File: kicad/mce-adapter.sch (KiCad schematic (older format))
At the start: 18 parts, among them U1 GAL16V8

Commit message: Add necroware kicad library
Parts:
- PWR1: footprint MyLibrary:USB_Mini-B-Jing_Extension_LSCS_C46398 -> Necroware:USB_Mini-B-Jing_Extension_LSCS_C46398
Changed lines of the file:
@@
 F 0 "PWR1" H 3657 1817 50  0000 C CNN
 F 1 "USB_B_Mini" H 3657 1726 50  0000 C CNN
-F 2 "MyLibrary:USB_Mini-B-Jing_Extension_LSCS_C46398" H 3750 1300 50  0001 C CNN
+F 2 "Necroware:USB_Mini-B-Jing_Extension_LSCS_C46398" H 3750 1300 50  0001 C CNN
 F 3 "~" H 3750 1300 50  0001 C CNN
 F 4 "C46398" H 3600 1350 50  0001 C CNN "LCSC"

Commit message: Vastly shrink PCB
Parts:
- R1, R2, R3: value 330 -> 470
- R4, R5, R6: value 220 -> 330
- renumbered JP1-3 to J123, JP4 to J4
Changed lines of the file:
@@
 P 5300 2750
 F 0 "R6" V 5250 2600 50  0000 C CNN
-F 1 "220" V 5300 2750 50  0000 C CNN
+F 1 "330" V 5300 2750 50  0000 C CNN
 F 2 "Resistor_THT:R_Axial_DIN0204_L3.6mm_D1.6mm_P7.62mm_Horizontal" V 5230 2750 50  0001 C CNN
 F 3 "~" H 5300 2750 50  0001 C CNN
@@
 P 4900 2650
 F 0 "R3" V 4850 2500 50  0000 C CNN
-F 1 "330" V 4900 2650 50  0000 C CNN
+F 1 "470" V 4900 2650 50  0000 C CNN
 F 2 "Resistor_THT:R_Axial_DIN0204_L3.6mm_D1.6mm_P7.62mm_Horizontal" V 4830 2650 50  0001 C CNN
 F 3 "~" H 4900 2650 50  0001 C CNN
@@
 P 5300 2550
 F 0 "R5" V 5250 2400 50  0000 C CNN
-F 1 "220" V 5300 2550 50  0000 C CNN
+F 1 "330" V 5300 2550 50  0000 C CNN
 F 2 "Resistor_THT:R_Axial_DIN0204_L3.6mm_D1.6mm_P7.62mm_Horizontal" V 5230 2550 50  0001 C CNN
 F 3 "~" H 5300 2550 50  0001 C CNN
@@
 P 5300 2350
 F 0 "R4" V 5250 2200 50  0000 C CNN
-F 1 "220" V 5300 2350 50  0000 C CNN
+F 1 "330" V 5300 2350 50  0000 C CNN
 F 2 "Resistor_THT:R_Axial_DIN0204_L3.6mm_D1.6mm_P7.62mm_Horizontal" V 5230 2350 50  0001 C CNN
 F 3 "~" H 5300 2350 50  0001 C CNN
@@
 P 4900 2450
 F 0 "R2" V 4850 2300 50  0000 C CNN
-F 1 "330" V 4900 2450 50  0000 C CNN
+F 1 "470" V 4900 2450 50  0000 C CNN
 F 2 "Resistor_THT:R_Axial_DIN0204_L3.6mm_D1.6mm_P7.62mm_Horizontal" V 4830 2450 50  0001 C CNN
 F 3 "~" H 4900 2450 50  0001 C CNN
@@
 	4100 1600 4100 1950
 $Comp
-L Connector:Conn_01x03_Male JP4
+L Connector:Conn_01x03_Male J4
 U 1 1 5FAB3B99
 P 3100 4300
-F 0 "JP4" H 3208 4581 50  0000 C CNN
+F 0 "J4" H 3208 4581 50  0000 C CNN
 F 1 "Conn_01x03_Male" H 3208 4490 50  0000 C CNN
 F 2 "Connector_PinHeader_2.54mm:PinHeader_1x03_P2.54mm_Vertical" H 3100 4300 50  0001 C CNN
@@
 P 4900 2250
 F 0 "R1" V 4850 2100 50  0000 C CNN
-F 1 "330" V 4900 2250 50  0000 C CNN
+F 1 "470" V 4900 2250 50  0000 C CNN
 F 2 "Resistor_THT:R_Axial_DIN0204_L3.6mm_D1.6mm_P7.62mm_Horizontal" V 4830 2250 50  0001 C CNN
 F 3 "~" H 4900 2250 50  0001 C CNN
@@
 $EndComp
 $Comp
-L Connector_Generic:Conn_02x03_Odd_Even JP1-3
-U 1 1 5FB500B7
-P 4350 4050
-F 0 "JP1-3" H 4400 4367 50  0000 C CNN
-F 1 "Conn_02x03_Odd_Even" H 4400 4276 50  0000 C CNN
-F 2 "Connector_PinHeader_2.54mm:PinHeader_2x03_P2.54mm_Vertical" H 4350 4050 50  0001 C CNN
-F 3 "~" H 4350 4050 50  0001 C CNN
-	1    4350 4050
-	1    0    0    -1
-$EndComp
-$Comp
 L power:GND #PWR0101
 U 1 1 5FB53A1F
@@
 	1    0    0    -1
 $EndComp
-Wire Wire Line
-	4650 3950 4650 4050
-Connection ~ 4650 4150
-Connection ~ 4650 4050
-Wire Wire Line
-	4650 4050 4650 4150
 $Comp
 L Connector:Conn_01x02_Male PWR2
@@
 	0    -1   1    0
 $EndComp
+Wire Wire Line
+	4650 3950 4650 4050
+Wire Wire Line
+	4650 4050 4650 4150
+Connection ~ 4650 4150
+Connection ~ 4650 4050
+$Comp
+L Connector_Generic:Conn_02x03_Odd_Even J123
+U 1 1 5FB500B7
+P 4350 4050
+F 0 "J123" H 4400 4367 50  0000 C CNN
+F 1 "Conn_02x03_Odd_Even" H 4400 4276 50  0000 C CNN
+F 2 "Connector_PinHeader_2.54mm:PinHeader_2x03_P2.54mm_Vertical" H 4350 4050 50  0001 C CNN
+F 3 "~" H 4350 4050 50  0001 C CNN
+	1    4350 4050
+	1    0    0    -1
+$EndComp
 $EndSCHEMATC

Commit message: Update LSCS part number
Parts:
- D1: LCSC Part (none) -> C402218
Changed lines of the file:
@@
 F 2 "Diode_THT:D_DO-34_SOD68_P10.16mm_Horizontal" H 4100 1350 50  0001 C CNN
 F 3 "~" H 4100 1350 50  0001 C CNN
+F 4 "C402218" V 4100 1350 50  0001 C CNN "LCSC Part"
 	1    4100 1350
 	0    -1   -1   0

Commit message: Update LCSC part numbers
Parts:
- C1: LCSC (none) -> C383039
- D1: LCSC (none) -> C402218; LCSC Part C402218 -> (none)
- H1: LCSC (none) -> C492405
- J123: LCSC (none) -> C65114
- J4: LCSC (none) -> C429954
- PWR2: LCSC (none) -> C152154
- R1, R2, R3: LCSC (none) -> C58592
- R4, R5, R6: LCSC (none) -> C58608
- R7, R8: LCSC (none) -> C57438
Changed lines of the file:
@@
 F 2 "Resistor_THT:R_Axial_DIN0204_L3.6mm_D1.6mm_P7.62mm_Horizontal" V 5230 2750 50  0001 C CNN
 F 3 "~" H 5300 2750 50  0001 C CNN
+F 4 "C58608" H 5300 2750 50  0001 C CNN "LCSC"
 	1    5300 2750
 	0    1    1    0
@@
 F 2 "Resistor_THT:R_Axial_DIN0204_L3.6mm_D1.6mm_P7.62mm_Horizontal" V 4830 2650 50  0001 C CNN
 F 3 "~" H 4900 2650 50  0001 C CNN
+F 4 "C58592" H 4900 2650 50  0001 C CNN "LCSC"
 	1    4900 2650
 	0    1    1    0
@@
 F 2 "Resistor_THT:R_Axial_DIN0204_L3.6mm_D1.6mm_P7.62mm_Horizontal" V 5230 2550 50  0001 C CNN
 F 3 "~" H 5300 2550 50  0001 C CNN
+F 4 "C58608" H 5300 2550 50  0001 C CNN "LCSC"
 	1    5300 2550
 	0    1    1    0
@@
 F 2 "Resistor_THT:R_Axial_DIN0204_L3.6mm_D1.6mm_P7.62mm_Horizontal" V 5230 2350 50  0001 C CNN
 F 3 "~" H 5300 2350 50  0001 C CNN
+F 4 "C58608" H 5300 2350 50  0001 C CNN "LCSC"
 	1    5300 2350
 	0    1    1    0
@@
 F 2 "Resistor_THT:R_Axial_DIN0204_L3.6mm_D1.6mm_P7.62mm_Horizontal" V 4830 2450 50  0001 C CNN
 F 3 "~" H 4900 2450 50  0001 C CNN
+F 4 "C58592" H 4900 2450 50  0001 C CNN "LCSC"
 	1    4900 2450
 	0    1    1    0
@@
 F 2 "Diode_THT:D_DO-34_SOD68_P10.16mm_Horizontal" H 4100 1350 50  0001 C CNN
 F 3 "~" H 4100 1350 50  0001 C CNN
-F 4 "C402218" V 4100 1350 50  0001 C CNN "LCSC Part"
+F 4 "C402218" V 4100 1350 50  0001 C CNN "LCSC"
 	1    4100 1350
 	0    -1   -1   0
@@
 F 2 "Resistor_THT:R_Axial_DIN0204_L3.6mm_D1.6mm_P7.62mm_Horizontal" V 4880 1600 50  0001 C CNN
 F 3 "~" H 4950 1600 50  0001 C CNN
+F 4 "C57438" H 4950 1600 50  0001 C CNN "LCSC"
 	1    4950 1600
 	0    1    1    0
@@
 F 2 "Connector_PinHeader_2.54mm:PinHeader_1x03_P2.54mm_Vertical" H 3100 4300 50  0001 C CNN
 F 3 "~" H 3100 4300 50  0001 C CNN
+F 4 "C429954" H 3100 4300 50  0001 C CNN "LCSC"
 	1    3100 4300
 	1    0    0    -1
@@
 F 2 "Connector_PinHeader_2.54mm:PinHeader_1x06_P2.54mm_Vertical" H 3100 3600 50  0001 C CNN
 F 3 "~" H 3100 3600 50  0001 C CNN
+F 4 "C492405" H 3100 3600 50  0001 C CNN "LCSC"
 	1    3100 3600
 	1    0    0    -1
@@
 F 2 "Resistor_THT:R_Axial_DIN0204_L3.6mm_D1.6mm_P7.62mm_Horizontal" V 4830 2150 50  0001 C CNN
 F 3 "~" H 4900 2150 50  0001 C CNN
+F 4 "C57438" H 4900 2150 50  0001 C CNN "LCSC"
 	1    4900 2150
 	0    1    1    0
@@
 F 2 "Resistor_THT:R_Axial_DIN0204_L3.6mm_D1.6mm_P7.62mm_Horizontal" V 4830 2250 50  0001 C CNN
 F 3 "~" H 4900 2250 50  0001 C CNN
+F 4 "C58592" H 4900 2250 50  0001 C CNN "LCSC"
 	1    4900 2250
 	0    1    1    0
@@
 F 2 "Capacitor_THT:CP_Radial_D5.0mm_P2.50mm" H 4438 1450 50  0001 C CNN
 F 3 "~" H 4400 1600 50  0001 C CNN
+F 4 "C383039" V 4400 1600 50  0001 C CNN "LCSC"
 	1    4400 1600
 	0    -1   -1   0
@@
 F 2 "Connector_PinHeader_2.54mm:PinHeader_1x02_P2.54mm_Vertical" H 4300 950 50  0001 C CNN
 F 3 "~" H 4300 950 50  0001 C CNN
+F 4 "C152154" H 4300 950 50  0001 C CNN "LCSC"
 	1    4300 950
 	0    -1   1    0
@@
 F 2 "Connector_PinHeader_2.54mm:PinHeader_2x03_P2.54mm_Vertical" H 4350 4050 50  0001 C CNN
 F 3 "~" H 4350 4050 50  0001 C CNN
+F 4 "C65114" H 4350 4050 50  0001 C CNN "LCSC"
 	1    4350 4050
 	1    0    0    -1

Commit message: Reajust some resistors improve layout
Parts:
- R1, R2, R3: value 470 -> 680
- R8: value 100 -> 1K
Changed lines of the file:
@@
 Sheet 1 1
 Title "MCE Adapter"
-Date "2020-11-11"
-Rev "0.7"
+Date "2020-12-06"
+Rev "0.7.1"
 Comp "Necroware"
 Comment1 "by Scorp"
@@
 P 4900 2650
 F 0 "R3" V 4850 2500 50  0000 C CNN
-F 1 "470" V 4900 2650 50  0000 C CNN
+F 1 "680" V 4900 2650 50  0000 C CNN
 F 2 "Resistor_THT:R_Axial_DIN0204_L3.6mm_D1.6mm_P7.62mm_Horizontal" V 4830 2650 50  0001 C CNN
 F 3 "~" H 4900 2650 50  0001 C CNN
@@
 P 4900 2450
 F 0 "R2" V 4850 2300 50  0000 C CNN
-F 1 "470" V 4900 2450 50  0000 C CNN
+F 1 "680" V 4900 2450 50  0000 C CNN
 F 2 "Resistor_THT:R_Axial_DIN0204_L3.6mm_D1.6mm_P7.62mm_Horizontal" V 4830 2450 50  0001 C CNN
 F 3 "~" H 4900 2450 50  0001 C CNN
@@
 P 4950 1600
 F 0 "R8" V 4850 1600 50  0000 C CNN
-F 1 "100" V 4950 1600 50  0000 C CNN
+F 1 "1K" V 4950 1600 50  0000 C CNN
 F 2 "Resistor_THT:R_Axial_DIN0204_L3.6mm_D1.6mm_P7.62mm_Horizontal" V 4880 1600 50  0001 C CNN
 F 3 "~" H 4950 1600 50  0001 C CNN
@@
 	4700 1600 4800 1600
 Wire Wire Line
-	5100 1600 5200 1600
-Wire Wire Line
-	5200 1600 5200 2150
-Wire Wire Line
-	5200 2150 5700 2150
+	5100 1600 5450 1600
+Wire Wire Line
+	5450 1600 5450 2150
+Wire Wire Line
+	5450 2150 5700 2150
 Text GLabel 4150 3950 0    50   Input ~ 0
 SW1_IN
@@
 $EndComp
 Wire Wire Line
-	5050 2150 5200 2150
-Connection ~ 5200 2150
+	5050 2150 5450 2150
+Connection ~ 5450 2150
 Wire Wire Line
 	4600 2150 4750 2150
@@
 P 4900 2250
 F 0 "R1" V 4850 2100 50  0000 C CNN
-F 1 "470" V 4900 2250 50  0000 C CNN
+F 1 "680" V 4900 2250 50  0000 C CNN
 F 2 "Resistor_THT:R_Axial_DIN0204_L3.6mm_D1.6mm_P7.62mm_Horizontal" V 4830 2250 50  0001 C CNN
 F 3 "~" H 4900 2250 50  0001 C CNN
@@
 	1    0    0    -1
 $EndComp
+Wire Wire Line
+	4700 1600 4700 1800
 $EndSCHEMATC

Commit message: Move parts away from VGA out.
Add some back face silk notations
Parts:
- D1: footprint Diode_THT:D_DO-34_SOD68_P10.16mm_Horizontal -> Diode_THT:D_DO-34_SOD68_P7.62mm_Horizontal
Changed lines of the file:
@@
 F 0 "D1" V 4146 1270 50  0000 R CNN
 F 1 "1N5819" V 4055 1270 50  0000 R CNN
-F 2 "Diode_THT:D_DO-34_SOD68_P10.16mm_Horizontal" H 4100 1350 50  0001 C CNN
+F 2 "Diode_THT:D_DO-34_SOD68_P7.62mm_Horizontal" H 4100 1350 50  0001 C CNN
 F 3 "~" H 4100 1350 50  0001 C CNN
 F 4 "C402218" V 4100 1350 50  0001 C CNN "LCSC"
@@
 	1    0    0    -1
 $EndComp
-Wire Wire Line
-	4700 1600 4700 1800
 $EndSCHEMATC

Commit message: Readjusted resistor values, updated to version 0.7.2
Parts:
- R1, R2, R3: value 680 -> 470
- R7: value 100 -> 75
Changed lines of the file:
@@
 Sheet 1 1
 Title "MCE Adapter"
-Date "2020-12-06"
-Rev "0.7.1"
+Date "2021-10-11"
+Rev "0.7.2"
 Comp "Necroware"
 Comment1 "by Scorp"
@@
 P 4900 2650
 F 0 "R3" V 4850 2500 50  0000 C CNN
-F 1 "680" V 4900 2650 50  0000 C CNN
+F 1 "470" V 4900 2650 50  0000 C CNN
 F 2 "Resistor_THT:R_Axial_DIN0204_L3.6mm_D1.6mm_P7.62mm_Horizontal" V 4830 2650 50  0001 C CNN
 F 3 "~" H 4900 2650 50  0001 C CNN
@@
 P 4900 2450
 F 0 "R2" V 4850 2300 50  0000 C CNN
-F 1 "680" V 4900 2450 50  0000 C CNN
+F 1 "470" V 4900 2450 50  0000 C CNN
 F 2 "Resistor_THT:R_Axial_DIN0204_L3.6mm_D1.6mm_P7.62mm_Horizontal" V 4830 2450 50  0001 C CNN
 F 3 "~" H 4900 2450 50  0001 C CNN
@@
 P 4900 2150
 F 0 "R7" V 4850 2000 50  0000 C CNN
-F 1 "100" V 4900 2150 50  0000 C CNN
+F 1 "75" V 4900 2150 50  0000 C CNN
 F 2 "Resistor_THT:R_Axial_DIN0204_L3.6mm_D1.6mm_P7.62mm_Horizontal" V 4830 2150 50  0001 C CNN
 F 3 "~" H 4900 2150 50  0001 C CNN
@@
 P 4900 2250
 F 0 "R1" V 4850 2100 50  0000 C CNN
-F 1 "680" V 4900 2250 50  0000 C CNN
+F 1 "470" V 4900 2250 50  0000 C CNN
 F 2 "Resistor_THT:R_Axial_DIN0204_L3.6mm_D1.6mm_P7.62mm_Horizontal" V 4830 2250 50  0001 C CNN
 F 3 "~" H 4900 2250 50  0001 C CNN

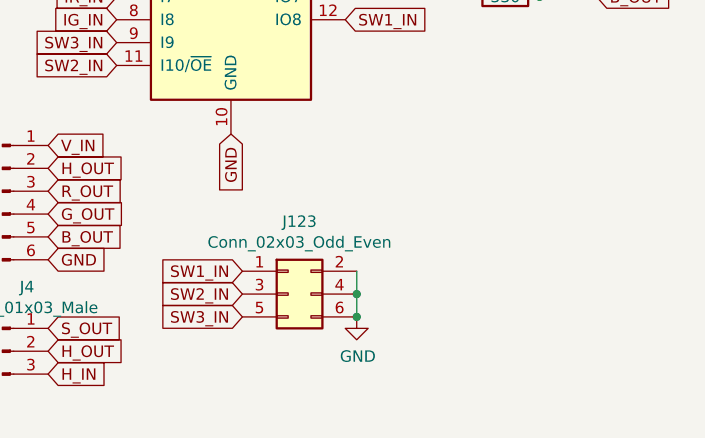
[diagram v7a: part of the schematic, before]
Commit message: Re-added DIP switch, rev. 0.8.0
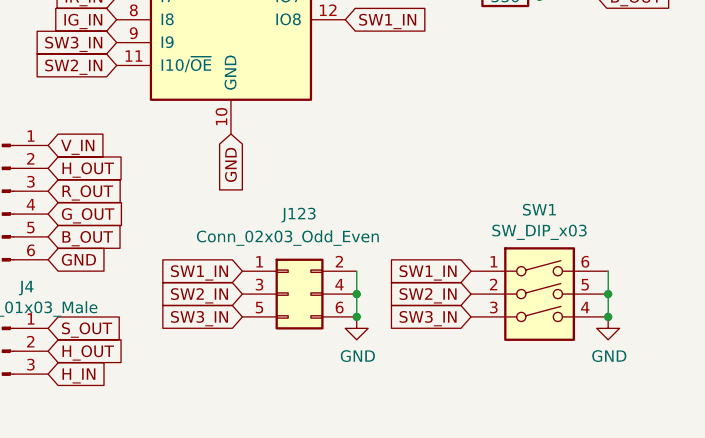
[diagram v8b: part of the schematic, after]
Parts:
- added SW1: SW_DIP_x03, Button_Switch_THT:SW_DIP_SPSTx03_Slide_9.78x9.8mm_W7.62mm_P2.54mm, symbol Switch:SW_DIP_x03
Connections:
- net GND: now also SW1.4, SW1.5, SW1.6
- net SW1_IN: now also SW1.1
- net SW2_IN: now also SW1.2
- net SW3_IN: now also SW1.3
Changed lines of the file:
@@
 Title "MCE Adapter"
 Date "2021-10-11"
-Rev "0.7.2"
+Rev "0.8.0"
 Comp "Necroware"
 Comment1 "by Scorp"
@@
 U 1 1 5FB500B7
 P 4350 4050
-F 0 "J123" H 4400 4367 50  0000 C CNN
-F 1 "Conn_02x03_Odd_Even" H 4400 4276 50  0000 C CNN
+F 0 "J123" H 4400 4400 50  0000 C CNN
+F 1 "Conn_02x03_Odd_Even" H 4350 4300 50  0000 C CNN
 F 2 "Connector_PinHeader_2.54mm:PinHeader_2x03_P2.54mm_Vertical" H 4350 4050 50  0001 C CNN
 F 3 "~" H 4350 4050 50  0001 C CNN
@@
 	1    0    0    -1
 $EndComp
+$Comp
+L Switch:SW_DIP_x03 SW1
+U 1 1 61643477
+P 5450 4150
+F 0 "SW1" H 5450 4617 50  0000 C CNN
+F 1 "SW_DIP_x03" H 5450 4526 50  0000 C CNN
+F 2 "Button_Switch_THT:SW_DIP_SPSTx03_Slide_9.78x9.8mm_W7.62mm_P2.54mm" H 5450 4150 50  0001 C CNN
+F 3 "~" H 5450 4150 50  0001 C CNN
+	1    5450 4150
+	1    0    0    -1
+$EndComp
+Text GLabel 5150 3950 0    50   Input ~ 0
+SW1_IN
+Text GLabel 5150 4050 0    50   Input ~ 0
+SW2_IN
+Text GLabel 5150 4150 0    50   Input ~ 0
+SW3_IN
+$Comp
+L power:GND #PWR0102
+U 1 1 61654423
+P 5750 4150
+F 0 "#PWR0102" H 5750 3900 50  0001 C CNN
+F 1 "GND" H 5755 3977 50  0000 C CNN
+F 2 "" H 5750 4150 50  0001 C CNN
+F 3 "" H 5750 4150 50  0001 C CNN
+	1    5750 4150
+	1    0    0    -1
+$EndComp
+Wire Wire Line
+	5750 3950 5750 4050
+Wire Wire Line
+	5750 4050 5750 4150
+Connection ~ 5750 4050
+Connection ~ 5750 4150
 $EndSCHEMATC
